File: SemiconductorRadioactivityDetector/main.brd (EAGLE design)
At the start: 27 parts, among them IC1 4011D, J1 22-05-7028-02, J2 22-05-7028-02, J3 22-05-7028-02, Q1 IRF530

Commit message: Initial unfinished version.
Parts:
- removed 11: CCFL_INVERTER_COIL, ccfl_inverter_coil:CCFL_INVERTER_COIL
- removed C10: 2n2/4k, resistor:C075-042X103
- removed C5: 100u/16V, resistor:153CLV-0505
- removed C8: 220n, resistor:C0805
- removed C9: 2n2/4k, rcl:C075-042X103
- removed D1, D2: GF1, diode:SMA-DO214AC
- removed D3: ES2D, diode:SMB
- removed D4, D5: BAV21, diode:DO35-10
- removed J2, J3: 22-05-7028-02, con-molex:7395-02
- removed Q1: IRF530, transistor-power:TO220BV
- removed SV1: (no value), con-lstb:MA05-1
- added C11: 100n, resistor:C1206
- added IC3: LM324N, linear:DIL14
- added R10, R11, R12, R6, R8, R9: 2k, resistor:M1206
- added R7: (no value), pot:B64Y
- C1: value 220n -> 100n; device resistor:C025-025X050 -> resistor:C1206
- C2: device resistor:C0805 -> resistor:C1206
- C4, C6: value 100u/16V -> 100n; device rcl:153CLV-0505 -> resistor:C1206
- C7: value 220n -> 100n; device resistor:C0805 -> resistor:C1206
- IC1: value 4011D -> 317T; device 40xx:SO14 -> linear:TO220H
- R1: value 4k7 -> 240R; device resistor:M0805 -> resistor:M1206
- R2, R3, R4: value 2k2 -> 2k; device resistor:M0805 -> resistor:M1206
- R5: value 33M -> 2k; device resistor:0207/10 -> resistor:M1206
- moved C6 147.7 mm to (-37.5, -108.6), flipped to the top, turned to 0 degrees
- moved R5 130.3 mm to (-29.8, -70.5), turned to 0 degrees
- moved C1 98.0 mm to (-29.8, -57.8), flipped to the top
- moved C4 94.0 mm to (-29.8, -64.1), flipped to the top, turned to 0 degrees
- moved R4 83.5 mm to (-29.8, -51.4), flipped to the top, turned to 0 degrees
- moved R3 76.7 mm to (-29.8, -45.1), flipped to the top, turned to 0 degrees
- moved R2 68.5 mm to (-29.8, -38.7), flipped to the top
- moved R1 66.2 mm to (-29.8, -33.7), flipped to the top
- moved IC1 57.5 mm to (-24.8, -18.4), flipped to the top, turned to 0 degrees
- renumbered J1 to POWER_SUPPLY
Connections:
- removed net N$22: IC1.3, IC1.5, IC1.6, R3.1, R4.1
- removed net N$23: C1.2, D1.A, D2.K, R2.2
- removed net N$24: D1.K, R3.2
- removed net N$25: D2.A, R4.2
- new net N$12: C6.1, IC3.13, R10.2, R11.1
- new net N$13: C6.2, IC3.14, R10.1
- new net N$14: IC3.12, R12.2
- new net N$8: C2.1, C3.+, IC1.3, POWER_SUPPLY.1
- new net N$9: R7.E, R9.2
- net GND: now also C1.2, C11.2, C4.2, IC3.11, R12.1, R2.1, R8.2; no longer C4.-, C5.-, C6.-, C8.2, IC1.7, Q1.S, SV1.1, SV1.2, SV1.3
- net N$1: now also IC1.1, R1.1, R2.2; no longer IC1.2, R2.1
- net N$10: now also R7.A, R8.1; no longer C10.2, D5.C, J2.1, J2.2, R5.2
- net N$11: now also IC3.9, R7.S; no longer 11.S2.A, 11.S2.B, C10.1, D4.A, J3.1, J3.2, R5.1
- net N$2: now also IC3.2, R3.2, R4.2; no longer IC1.1, R1.2, SV1.4
- net N$3: now also IC3.1, IC3.5, R3.1; no longer 11.P2, D3.A, Q1.D
- net N$4: now also C1.1, R4.1; no longer IC1.10, IC1.11, Q1.G
- net N$5: now also IC3.6, R5.2, R6.2; no longer C1.1, IC1.12, IC1.13, IC1.4, IC1.8, IC1.9
- net N$6: now also IC3.10, IC3.7, R11.2, R5.1; no longer 11.S1.A, 11.S1.B, C9.1
- net N$7: now also C4.1, R6.1; no longer C9.2, D4.C, D5.A
- net VCC: now also C11.1, IC1.2, IC3.4, R1.2, R9.1; no longer 11.P1, C2.1, C3.+, C4.+, C5.+, C6.+, C8.1, D3.C, IC1.14, POWER_SUPPLY.1, R1.1, SV1.5
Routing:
- net VCC: track 88.8 -> 19.5 mm
- net N$2: track 42.5 -> 0.00 mm
- net N$10: track 39.6 -> 0.00 mm
- net N$11: track 39.4 -> 0.00 mm
- net N$6: track 26.7 -> 0.00 mm
- net N$23: track 22.7 -> 0.00 mm
- net N$4: track 21.5 -> 0.00 mm, vias 2 -> 0
- net N$3: track 18.2 -> 0.00 mm
- net N$5: track 17.7 -> 0.00 mm
- net N$22: track 12.0 -> 0.00 mm
- net N$7: track 9.42 -> 0.00 mm
- net N$1: track 4.76 -> 0.00 mm
- net N$8: track 0.00 -> 4.25 mm
- net N$25: track 2.71 -> 0.00 mm
- net N$24: track 2.71 -> 0.00 mm

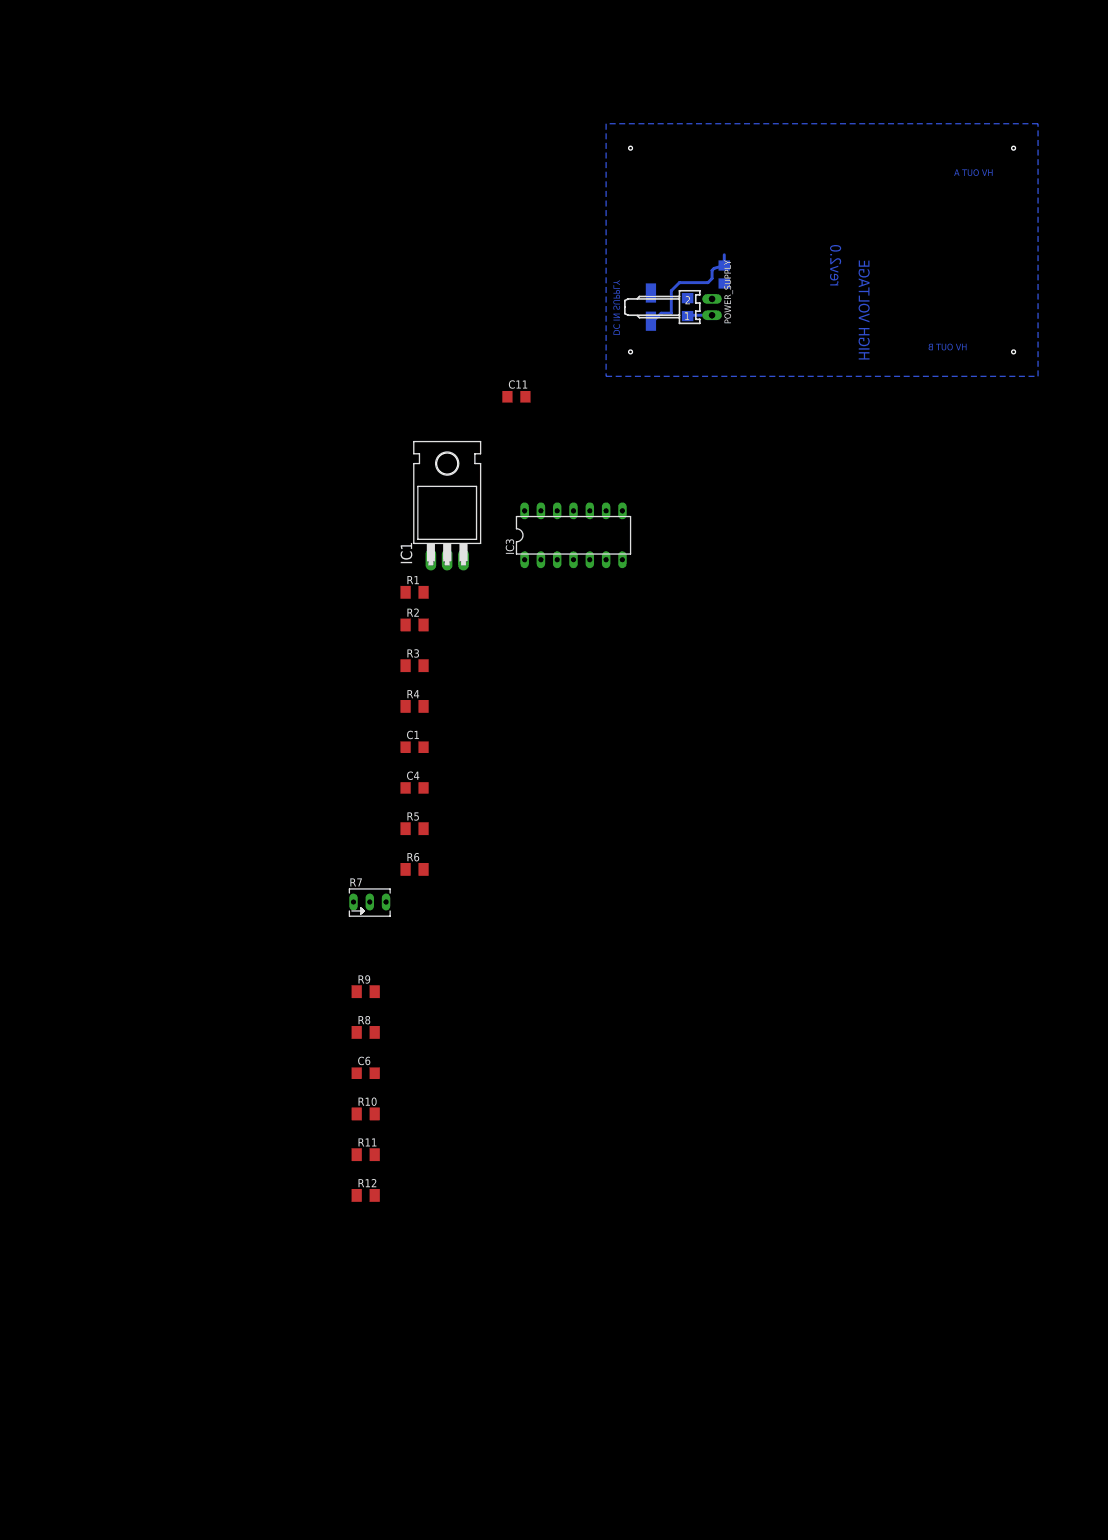
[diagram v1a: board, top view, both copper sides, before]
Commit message: Initial version,  PCB not done.
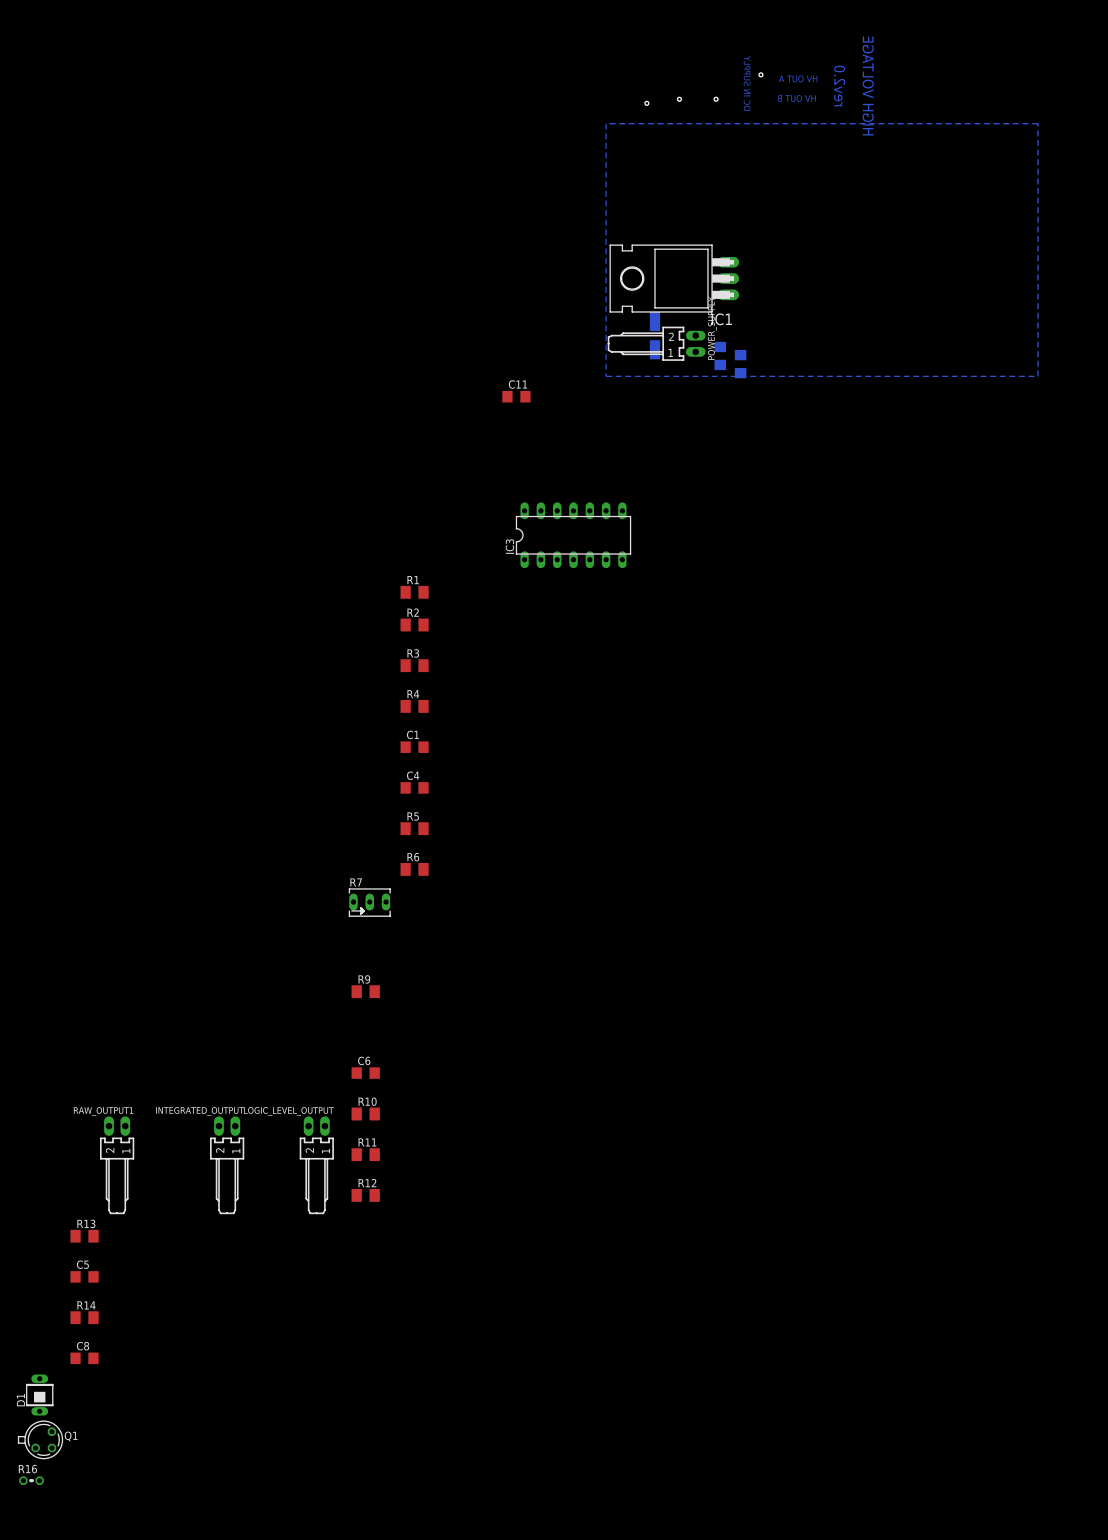
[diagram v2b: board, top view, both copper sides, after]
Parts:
- removed R8: 2k, resistor:M1206
- added C5, C8: 100n, resistor:C1206
- added D1: BP104, opto-trans-siemens:BP104
- added INTEGRATED_OUTPUT, LOGIC_LEVEL_OUTPUT, RAW_OUTPUT1: 22-05-7028-02, con-molex:7395-02
- added Q1: 2N4093, transistor-fet:TO18
- added R13: 1M, resistor:M1206
- added R14: 47k, resistor:M1206
- added R16: 10M, resistor:0204V
- C1, C4: value 100n -> 15n
- R10, R3: value 2k -> 1M
- R11, R12, R5: value 2k -> 100k
- R4, R6: value 2k -> 1k
- R7: value (none) -> 1k
- R9: value 2k -> 4k7
- moved IC1 47.6 mm to (8.89, 15.2), turned to 90 degrees
- moved C7 14.2 mm to (21.0, 1.91)
- moved C2 9.16 mm to (17.8, 3.17)
- moved POWER_SUPPLY 6.25 mm to (14.0, 5.08)
- moved C3 4.49 mm to (7.62, 6.35)
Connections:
- removed net N$10: R7.A, R8.1
- removed net N$6: IC3.10, IC3.7, R11.2, R5.1
- new net N$15: IC3.8, LOGIC_LEVEL_OUTPUT.2
- new net N$16: C5.1, D1.K, R13.2
- new net N$17: D1.A, Q1.3, R16.1
- new net N$18: IC3.3, Q1.2, R14.1
- new net N$19: IC3.10, IC3.7, R11.2, R5.1, RAW_OUTPUT1.1
- net GND: now also C5.2, C8.2, INTEGRATED_OUTPUT.2, LOGIC_LEVEL_OUTPUT.1, Q1.1, R16.2, R7.A, RAW_OUTPUT1.2; no longer R8.2
- net N$13: now also INTEGRATED_OUTPUT.1
- net VCC: now also C8.1, R13.1, R14.2
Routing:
- net VCC: track 19.5 -> 0.00 mm
- net N$8: track 4.25 -> 0.00 mm

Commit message: Power supply done.
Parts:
- added C9: 100n, resistor:C1206
- moved R1 59.7 mm to (13.3, 7.62), flipped to the bottom, turned to 180 degrees
- moved R2 58.8 mm to (10.8, 3.81), flipped to the bottom, turned to 180 degrees
- moved C2 11.5 mm to (19.1, 14.6)
- moved C7 11.4 mm to (14.6, 11.4), turned to 0 degrees
- moved POWER_SUPPLY 10.9 mm to (15.2, 15.9)
- moved IC1 8.25 mm to (8.89, 6.99)
- moved C3 7.10 mm to (8.89, 13.3), turned to 90 degrees
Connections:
- net N$12: now also C9.1
- net N$13: now also C9.2
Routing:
- net N$8: track 0.00 -> 14.8 mm
- net N$1: track 0.00 -> 11.0 mm
- net VCC: track 0.00 -> 8.44 mm
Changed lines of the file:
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@@
 </autorouter>
 <elements>
-<element name="C7" library="resistor" package="C1206" value="100n" x="20.955" y="1.905" rot="MR270"/>
-<element name="C2" library="resistor" package="C1206" value="100n" x="17.78" y="3.175" rot="MR90"/>
-<element name="C3" library="rcl" package="153CLV-0505" value="100u/16V" x="7.62" y="6.35" rot="MR270"/>
-<element name="POWER_SUPPLY" library="con-molex" package="7395-02" value="22-05-7028-02" x="13.97" y="5.08" rot="R270">
-<attribute name="MF" value="" x="13.97" y="5.08" size="1.778" layer="27" rot="R270" display="off"/>
-<attribute name="OC_NEWARK" value="unknown" x="13.97" y="5.08" size="1.778" layer="27" rot="R270" display="off"/>
-<attribute name="OC_FARNELL" value="9731601" x="13.97" y="5.08" size="1.778" layer="27" rot="R270" display="off"/>
-<attribute name="MPN" value="" x="13.97" y="5.08" size="1.778" layer="27" rot="R270" display="off"/>
+<element name="C7" library="resistor" package="C1206" value="100n" x="14.605" y="11.43" rot="MR0"/>
+<element name="C2" library="resistor" package="C1206" value="100n" x="19.05" y="14.605" rot="MR90"/>
+<element name="C3" library="rcl" package="153CLV-0505" value="100u/16V" x="8.89" y="13.335" rot="MR90"/>
+<element name="POWER_SUPPLY" library="con-molex" package="7395-02" value="22-05-7028-02" x="15.24" y="15.875" rot="R270">
+<attribute name="MF" value="" x="15.24" y="15.875" size="1.778" layer="27" rot="R270" display="off"/>
+<attribute name="OC_NEWARK" value="unknown" x="15.24" y="15.875" size="1.778" layer="27" rot="R270" display="off"/>
+<attribute name="OC_FARNELL" value="9731601" x="15.24" y="15.875" size="1.778" layer="27" rot="R270" display="off"/>
+<attribute name="MPN" value="" x="15.24" y="15.875" size="1.778" layer="27" rot="R270" display="off"/>
 </element>
 <element name="C11" library="resistor" package="C1206" value="100n" x="-13.97" y="-3.175"/>
 <element name="IC3" library="linear" package="DIL14" value="LM324N" x="-5.08" y="-24.765"/>
-<element name="IC1" library="linear" package="TO220H" value="317T" x="8.89" y="15.24" rot="R90"/>
-<element name="R1" library="resistor" package="M1206" value="240R" x="-29.845" y="-33.655"/>
-<element name="R2" library="resistor" package="M1206" value="2k" x="-29.845" y="-38.735"/>
+<element name="IC1" library="linear" package="TO220H" value="317T" x="8.89" y="6.985" rot="R90"/>
+<element name="R1" library="resistor" package="M1206" value="240R" x="13.335" y="7.62" rot="MR180"/>
+<element name="R2" library="resistor" package="M1206" value="2k" x="10.795" y="3.81" rot="MR180"/>
 <element name="R3" library="resistor" package="M1206" value="1M" x="-29.845" y="-45.085"/>
 <element name="R4" library="resistor" package="M1206" value="1k" x="-29.845" y="-51.435"/>
@@
 <element name="Q1" library="transistor-fet" package="TO18" value="2N4093" x="-87.63" y="-165.735"/>
 <element name="R16" library="resistor" package="0204V" value="10M" x="-89.535" y="-172.085"/>
+<element name="C9" library="resistor" package="C1206" value="100n" x="-89.535" y="-178.435"/>
 </elements>
 <signals>
@@
 <contactref element="R14" pad="2"/>
 <contactref element="C8" pad="1"/>
+<wire x1="19.05" y1="6.985" x2="17.145" y2="6.985" width="0.6096" layer="16"/>
+<wire x1="17.145" y1="6.985" x2="16.51" y2="7.62" width="0.6096" layer="16"/>
+<wire x1="16.51" y1="7.62" x2="15.875" y2="7.62" width="0.6096" layer="16"/>
+<wire x1="15.875" y1="7.62" x2="14.735" y2="7.62" width="0.6096" layer="16"/>
+<wire x1="16.005" y1="11.43" x2="16.005" y2="7.75" width="0.6096" layer="16"/>
+<wire x1="16.005" y1="7.75" x2="15.875" y2="7.62" width="0.6096" layer="16"/>
 <wire x1="-79.88" y1="-146.685" x2="-82.68" y2="-153.035" width="0" layer="19" extent="1-1"/>
 <wire x1="-82.68" y1="-133.985" x2="-79.88" y2="-146.685" width="0" layer="19" extent="1-1"/>
 <wire x1="-38.865" y1="-95.885" x2="-82.68" y2="-133.985" width="0" layer="19" extent="1-1"/>
-<wire x1="-28.445" y1="-33.655" x2="-38.865" y2="-95.885" width="0" layer="19" extent="1-1"/>
-<wire x1="-5.08" y1="-28.575" x2="-28.445" y2="-33.655" width="0" layer="19" extent="1-1"/>
+<wire x1="-5.08" y1="-28.575" x2="-38.865" y2="-95.885" width="0" layer="19" extent="1-1"/>
 <wire x1="-15.37" y1="-3.175" x2="-5.08" y2="-28.575" width="0" layer="19" extent="1-1"/>
-<wire x1="20.955" y1="3.305" x2="-15.37" y2="-3.175" width="0" layer="19" extent="1-16"/>
-<wire x1="19.05" y1="15.24" x2="20.955" y2="3.305" width="0" layer="19" extent="16-16"/>
+<wire x1="14.735" y1="7.62" x2="-15.37" y2="-3.175" width="0" layer="19" extent="1-16"/>
 </signal>
 <signal name="GND">
@@
 <wire x1="-28.445" y1="-64.135" x2="-34.29" y2="-81.915" width="0" layer="19" extent="1-1"/>
 <wire x1="-28.445" y1="-57.785" x2="-28.445" y2="-64.135" width="0" layer="19" extent="1-1"/>
-<wire x1="-31.245" y1="-38.735" x2="-28.445" y2="-57.785" width="0" layer="19" extent="1-1"/>
-<wire x1="-5.08" y1="-20.955" x2="-31.245" y2="-38.735" width="0" layer="19" extent="1-1"/>
+<wire x1="-5.08" y1="-20.955" x2="-28.445" y2="-57.785" width="0" layer="19" extent="1-1"/>
 <wire x1="-12.57" y1="-3.175" x2="-5.08" y2="-20.955" width="0" layer="19" extent="1-1"/>
-<wire x1="7.62" y1="8.55" x2="-12.57" y2="-3.175" width="0" layer="19" extent="1-16"/>
+<wire x1="9.395" y1="3.81" x2="-12.57" y2="-3.175" width="0" layer="19" extent="1-16"/>
 </signal>
 <signal name="N$8">
@@
 <contactref element="POWER_SUPPLY" pad="1"/>
 <contactref element="IC1" pad="3"/>
-<wire x1="13.97" y1="3.81" x2="19.05" y2="17.78" width="0" layer="19" extent="1-1"/>
-<wire x1="17.78" y1="1.775" x2="13.97" y2="3.81" width="0" layer="19" extent="16-16"/>
-<wire x1="7.62" y1="4.15" x2="13.97" y2="3.81" width="0" layer="19" extent="16-16"/>
+<wire x1="15.24" y1="14.605" x2="16.51" y2="14.605" width="0.6096" layer="16"/>
+<wire x1="16.51" y1="14.605" x2="17.78" y2="13.335" width="0.6096" layer="16"/>
+<wire x1="17.78" y1="13.335" x2="18.92" y2="13.335" width="0.6096" layer="16"/>
+<wire x1="18.92" y1="13.335" x2="19.05" y2="13.205" width="0.6096" layer="16"/>
+<wire x1="19.05" y1="13.205" x2="19.05" y2="9.525" width="0.6096" layer="16"/>
+<wire x1="15.24" y1="14.605" x2="12.065" y2="14.605" width="0.6096" layer="16"/>
+<wire x1="12.065" y1="14.605" x2="11.43" y2="15.24" width="0.6096" layer="16"/>
+<wire x1="11.43" y1="15.24" x2="9.185" y2="15.24" width="0.6096" layer="16"/>
+<wire x1="9.185" y1="15.24" x2="8.89" y2="15.535" width="0.6096" layer="16"/>
 </signal>
 <signal name="N$1">
@@
 <contactref element="R1" pad="1"/>
 <contactref element="R2" pad="2"/>
-<wire x1="-31.245" y1="-33.655" x2="-28.445" y2="-38.735" width="0" layer="19" extent="1-1"/>
-<wire x1="19.05" y1="12.7" x2="-31.245" y2="-33.655" width="0" layer="19" extent="1-1"/>
+<wire x1="19.05" y1="4.445" x2="16.51" y2="4.445" width="0.6096" layer="16"/>
+<wire x1="16.51" y1="4.445" x2="15.875" y2="3.81" width="0.6096" layer="16"/>
+<wire x1="15.875" y1="3.81" x2="12.195" y2="3.81" width="0.6096" layer="16"/>
+<wire x1="12.195" y1="3.81" x2="12.195" y2="5.585" width="0.6096" layer="16"/>
+<wire x1="12.195" y1="5.585" x2="12.065" y2="5.715" width="0.6096" layer="16"/>
+<wire x1="12.065" y1="5.715" x2="12.065" y2="7.49" width="0.6096" layer="16"/>
+<wire x1="12.065" y1="7.49" x2="11.935" y2="7.62" width="0.6096" layer="16"/>
 </signal>
 <signal name="N$2">
@@
 <contactref element="R10" pad="2"/>
 <contactref element="R11" pad="1"/>
+<contactref element="C9" pad="1"/>
 <wire x1="-36.065" y1="-114.935" x2="-38.865" y2="-121.285" width="0" layer="19" extent="1-1"/>
 <wire x1="-38.865" y1="-108.585" x2="-36.065" y2="-114.935" width="0" layer="19" extent="1-1"/>
+<wire x1="-90.935" y1="-178.435" x2="-38.865" y2="-121.285" width="0" layer="19" extent="1-1"/>
 <wire x1="-10.16" y1="-20.955" x2="-38.865" y2="-108.585" width="0" layer="19" extent="1-1"/>
 </signal>
@@
 <contactref element="R10" pad="1"/>
 <contactref element="INTEGRATED_OUTPUT" pad="1"/>
+<contactref element="C9" pad="2"/>
 <wire x1="-38.865" y1="-114.935" x2="-57.785" y2="-116.84" width="0" layer="19" extent="1-1"/>
 <wire x1="-36.065" y1="-108.585" x2="-38.865" y2="-114.935" width="0" layer="19" extent="1-1"/>
+<wire x1="-88.135" y1="-178.435" x2="-57.785" y2="-116.84" width="0" layer="19" extent="1-1"/>
 <wire x1="-12.7" y1="-20.955" x2="-36.065" y2="-108.585" width="0" layer="19" extent="1-1"/>
 </signal>
